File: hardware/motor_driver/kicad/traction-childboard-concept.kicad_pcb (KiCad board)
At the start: 2 copper layers, 118 x 82 mm, 4 parts

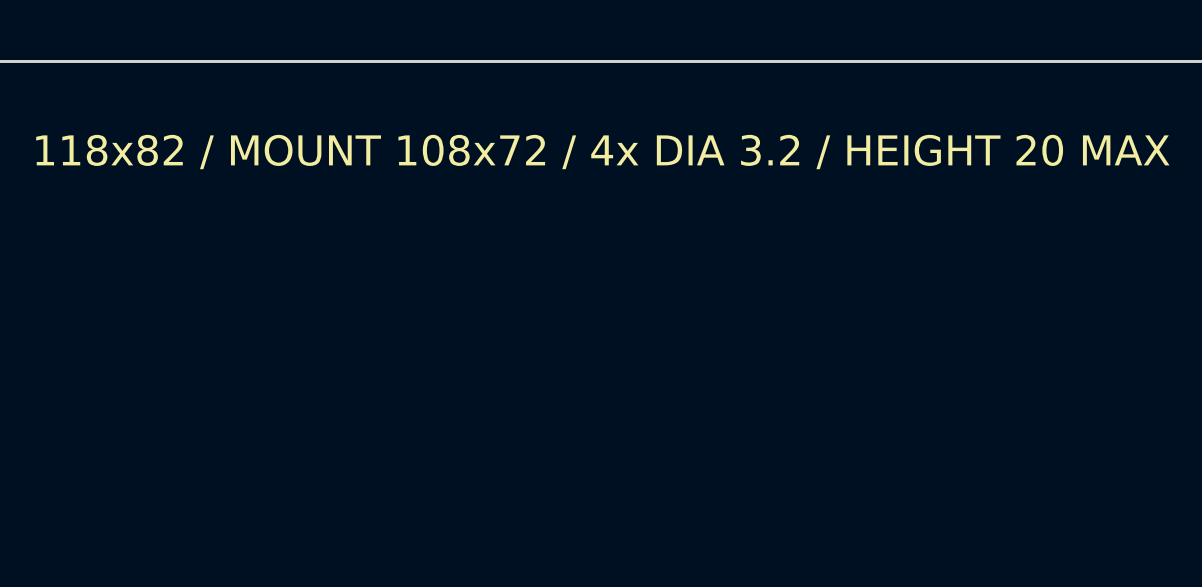
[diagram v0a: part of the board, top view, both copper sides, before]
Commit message: feat(hardware): close traction interfaces and release gates
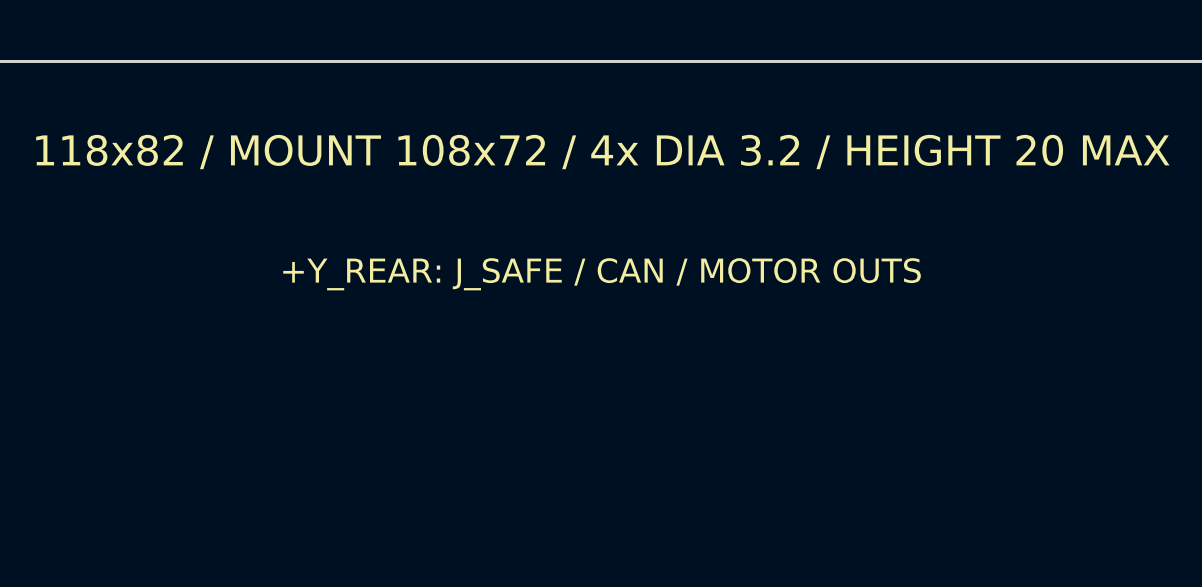
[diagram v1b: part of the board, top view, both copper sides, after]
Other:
- board text added: "+Y_REAR: J_SAFE / CAN / MOTOR OUTS"
- board text added: "J_CAN"
- board text added: "J_SAFE"
- board text removed: "CAN"
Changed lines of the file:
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@@
 	(title_block
 		(title "Workbench-1 Dual-Axis Traction Childboard Mechanical Concept")
-		(rev "CONCEPT-A")
+		(rev "CONCEPT-B")
 	)
 	(layers
@@
 	)
 	(gr_line
-		(start 10 19)
-		(end 10 7)
-		(stroke
-			(width 0.2)
-			(type default)
-		)
-		(layer "F.Fab")
-	)
-	(gr_line
-		(start 10 7)
-		(end 24 7)
-		(stroke
-			(width 0.2)
-			(type default)
-		)
-		(layer "F.Fab")
-	)
-	(gr_line
 		(start 100 15)
 		(end 100 7)
@@
 	)
 	(gr_line
-		(start 107 19)
-		(end 117 19)
-		(stroke
-			(width 0.2)
-			(type default)
-		)
-		(layer "F.Fab")
-	)
-	(gr_line
-		(start 107 35)
-		(end 107 19)
-		(stroke
-			(width 0.2)
-			(type default)
-		)
-		(layer "F.Fab")
-	)
-	(gr_line
-		(start 107 49)
-		(end 117 49)
-		(stroke
-			(width 0.2)
-			(type default)
-		)
-		(layer "F.Fab")
-	)
-	(gr_line
-		(start 107 65)
-		(end 107 49)
+		(start 100 72)
+		(end 110 72)
+		(stroke
+			(width 0.2)
+			(type default)
+		)
+		(layer "F.Fab")
+	)
+	(gr_line
+		(start 100 82)
+		(end 100 72)
 		(stroke
 			(width 0.2)
@@
 	)
 	(gr_line
-		(start 117 19)
-		(end 117 35)
-		(stroke
-			(width 0.2)
-			(type default)
-		)
-		(layer "F.Fab")
-	)
-	(gr_line
-		(start 117 35)
-		(end 107 35)
-		(stroke
-			(width 0.2)
-			(type default)
-		)
-		(layer "F.Fab")
-	)
-	(gr_line
-		(start 117 49)
-		(end 117 65)
-		(stroke
-			(width 0.2)
-			(type default)
-		)
-		(layer "F.Fab")
-	)
-	(gr_line
-		(start 117 65)
-		(end 107 65)
+		(start 110 72)
+		(end 110 82)
+		(stroke
+			(width 0.2)
+			(type default)
+		)
+		(layer "F.Fab")
+	)
+	(gr_line
+		(start 110 82)
+		(end 100 82)
 		(stroke
 			(width 0.2)
@@
 	)
 	(gr_line
+		(start 12 74)
+		(end 24 74)
+		(stroke
+			(width 0.2)
+			(type default)
+		)
+		(layer "F.Fab")
+	)
+	(gr_line
+		(start 12 82)
+		(end 12 74)
+		(stroke
+			(width 0.2)
+			(type default)
+		)
+		(layer "F.Fab")
+	)
+	(gr_line
 		(start 15 31)
 		(end 15 51)
@@
 	)
 	(gr_line
-		(start 24 19)
-		(end 10 19)
-		(stroke
-			(width 0.2)
-			(type default)
-		)
-		(layer "F.Fab")
-	)
-	(gr_line
-		(start 24 7)
-		(end 24 19)
+		(start 24 74)
+		(end 24 82)
+		(stroke
+			(width 0.2)
+			(type default)
+		)
+		(layer "F.Fab")
+	)
+	(gr_line
+		(start 24 82)
+		(end 12 82)
 		(stroke
 			(width 0.2)
@@
 	)
 	(gr_line
+		(start 30 74)
+		(end 44 74)
+		(stroke
+			(width 0.2)
+			(type default)
+		)
+		(layer "F.Fab")
+	)
+	(gr_line
+		(start 30 82)
+		(end 30 74)
+		(stroke
+			(width 0.2)
+			(type default)
+		)
+		(layer "F.Fab")
+	)
+	(gr_line
 		(start 31 34)
 		(end 39 34)
@@
 	)
 	(gr_line
+		(start 44 74)
+		(end 44 82)
+		(stroke
+			(width 0.2)
+			(type default)
+		)
+		(layer "F.Fab")
+	)
+	(gr_line
+		(start 44 82)
+		(end 30 82)
+		(stroke
+			(width 0.2)
+			(type default)
+		)
+		(layer "F.Fab")
+	)
+	(gr_line
 		(start 49 19)
 		(end 29 19)
@@
 	)
 	(gr_line
+		(start 73 72)
+		(end 83 72)
+		(stroke
+			(width 0.2)
+			(type default)
+		)
+		(layer "F.Fab")
+	)
+	(gr_line
+		(start 73 82)
+		(end 73 72)
+		(stroke
+			(width 0.2)
+			(type default)
+		)
+		(layer "F.Fab")
+	)
+	(gr_line
 		(start 77 18)
 		(end 59 18)
@@
 	)
 	(gr_line
+		(start 83 72)
+		(end 83 82)
+		(stroke
+			(width 0.2)
+			(type default)
+		)
+		(layer "F.Fab")
+	)
+	(gr_line
+		(start 83 82)
+		(end 73 82)
+		(stroke
+			(width 0.2)
+			(type default)
+		)
+		(layer "F.Fab")
+	)
+	(gr_line
 		(start 87 15)
 		(end 87 7)
@@
 		)
 		(layer "F.Fab")
+	)
+	(gr_text "+Y_REAR: J_SAFE / CAN / MOTOR OUTS"
+		(at 59 7 0)
+		(layer "F.SilkS")
+		(effects
+			(font
+				(size 0.8 0.8)
+				(thickness 0.15)
+			)
+		)
 	)
 	(gr_text "118x82 / MOUNT 108x72 / 4x DIA 3.2 / HEIGHT 20 MAX"
@@
 		)
 	)
-	(gr_text "CAN"
-		(at 17 13 0)
-		(layer "F.Fab")
-		(effects
-			(font
-				(size 1.2 1.2)
-				(thickness 0.15)
-			)
-		)
-	)
 	(gr_text "CLAMP"
 		(at 47 62 0)
@@
 		)
 	)
+	(gr_text "J_CAN"
+		(at 37 78 0)
+		(layer "F.Fab")
+		(effects
+			(font
+				(size 1.2 1.2)
+				(thickness 0.15)
+			)
+		)
+	)
 	(gr_text "J_ENC_L"
 		(at 92 11 0)
@@
 	)
 	(gr_text "J_ML"
-		(at 112 27 0)
+		(at 78 77 0)
 		(layer "F.Fab")
 		(effects
@@
 	)
 	(gr_text "J_MR"
-		(at 112 57 0)
+		(at 105 77 0)
 		(layer "F.Fab")
 		(effects
@@
 		(layer "F.Fab")
 		(effects
+			(font
+				(size 1.2 1.2)
+				(thickness 0.15)
+			)
+		)
+	)
+	(gr_text "J_SAFE"
+		(at 18 78 0)
+		(layer "F.Fab")
+		(effects
